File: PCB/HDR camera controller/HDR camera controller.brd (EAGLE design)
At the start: 58 x 48 mm, 63 parts, among them IC1 USBLC6-4, IC10 RS422-SO8, IC11 RS422-SO8, IC12 USBLC6-4, IC14 741G157, IC2 RS422-SO8, IC3 RS422-SO8, IC4 RS422-SO8, IC6 FT232RL, IC7 74HC00D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

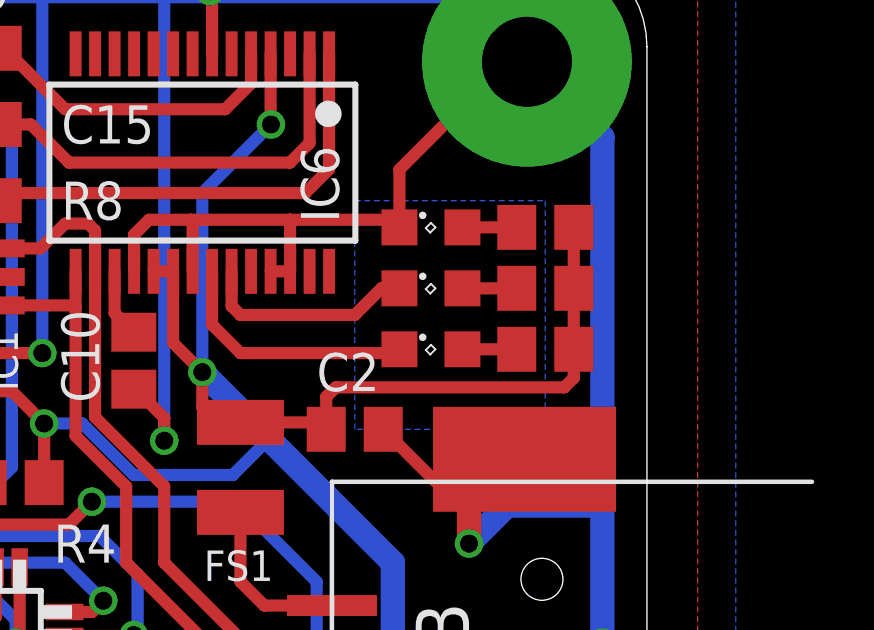
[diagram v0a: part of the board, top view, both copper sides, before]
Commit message: amogus did not print, got rid of it :(
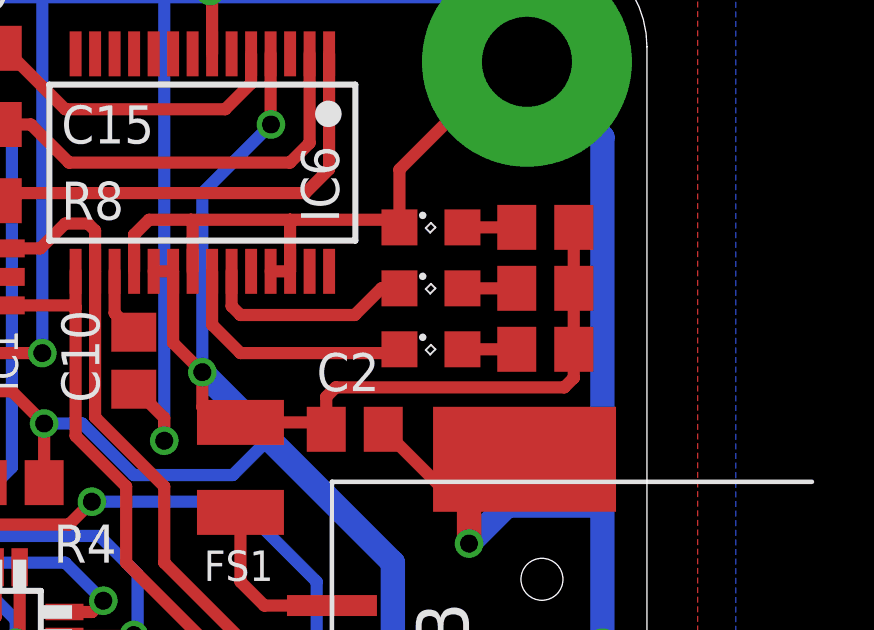
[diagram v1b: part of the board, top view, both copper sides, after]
